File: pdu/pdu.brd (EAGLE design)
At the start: 0 parts

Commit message: import outline from fusion, add mounts
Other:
- board outline added: 17.5 x 90 mm
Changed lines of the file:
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@@
 <setting verticaltext="up"/>
 </settings>
-<grid distance="50" unitdist="mil" unit="mil" style="lines" multiple="1" display="no" altdistance="5" altunitdist="mil" altunit="mil"/>
+<grid distance="50" unitdist="mil" unit="mil" style="lines" multiple="1" display="yes" altdistance="5" altunitdist="mil" altunit="mil"/>
 <layers>
 <layer number="1" name="Top" color="4" fill="1" visible="yes" active="yes"/>
@@
 <layer number="18" name="Vias" color="2" fill="1" visible="yes" active="yes"/>
 <layer number="19" name="Unrouted" color="6" fill="1" visible="yes" active="yes"/>
-<layer number="20" name="Dimension" color="24" fill="1" visible="yes" active="yes"/>
-<layer number="21" name="tPlace" color="7" fill="1" visible="yes" active="yes"/>
-<layer number="22" name="bPlace" color="7" fill="1" visible="yes" active="yes"/>
+<layer number="20" name="Dimension" color="15" fill="1" visible="yes" active="yes"/>
+<layer number="21" name="tPlace" color="16" fill="1" visible="yes" active="yes"/>
+<layer number="22" name="bPlace" color="14" fill="1" visible="yes" active="yes"/>
 <layer number="23" name="tOrigins" color="15" fill="1" visible="yes" active="yes"/>
 <layer number="24" name="bOrigins" color="15" fill="1" visible="yes" active="yes"/>
-<layer number="25" name="tNames" color="7" fill="1" visible="yes" active="yes"/>
-<layer number="26" name="bNames" color="7" fill="1" visible="yes" active="yes"/>
-<layer number="27" name="tValues" color="7" fill="1" visible="yes" active="yes"/>
-<layer number="28" name="bValues" color="7" fill="1" visible="yes" active="yes"/>
+<layer number="25" name="tNames" color="7" fill="1" visible="no" active="yes"/>
+<layer number="26" name="bNames" color="7" fill="1" visible="no" active="yes"/>
+<layer number="27" name="tValues" color="7" fill="1" visible="no" active="yes"/>
+<layer number="28" name="bValues" color="7" fill="1" visible="no" active="yes"/>
 <layer number="29" name="tStop" color="7" fill="3" visible="no" active="yes"/>
 <layer number="30" name="bStop" color="7" fill="6" visible="no" active="yes"/>
@@
 <layer number="37" name="tTest" color="7" fill="1" visible="no" active="yes"/>
 <layer number="38" name="bTest" color="7" fill="1" visible="no" active="yes"/>
-<layer number="39" name="tKeepout" color="4" fill="11" visible="yes" active="yes"/>
-<layer number="40" name="bKeepout" color="1" fill="11" visible="yes" active="yes"/>
-<layer number="41" name="tRestrict" color="4" fill="10" visible="yes" active="yes"/>
-<layer number="42" name="bRestrict" color="1" fill="10" visible="yes" active="yes"/>
-<layer number="43" name="vRestrict" color="2" fill="10" visible="yes" active="yes"/>
+<layer number="39" name="tKeepout" color="4" fill="11" visible="no" active="yes"/>
+<layer number="40" name="bKeepout" color="1" fill="11" visible="no" active="yes"/>
+<layer number="41" name="tRestrict" color="4" fill="10" visible="no" active="yes"/>
+<layer number="42" name="bRestrict" color="1" fill="10" visible="no" active="yes"/>
+<layer number="43" name="vRestrict" color="2" fill="10" visible="no" active="yes"/>
 <layer number="44" name="Drills" color="7" fill="1" visible="no" active="yes"/>
-<layer number="45" name="Holes" color="7" fill="1" visible="no" active="yes"/>
+<layer number="45" name="Holes" color="7" fill="1" visible="yes" active="yes"/>
 <layer number="46" name="Milling" color="3" fill="1" visible="no" active="yes"/>
 <layer number="47" name="Measures" color="7" fill="1" visible="no" active="yes"/>
-<layer number="48" name="Document" color="7" fill="1" visible="yes" active="yes"/>
-<layer number="49" name="Reference" color="7" fill="1" visible="yes" active="yes"/>
-<layer number="51" name="tDocu" color="7" fill="1" visible="yes" active="yes"/>
-<layer number="52" name="bDocu" color="7" fill="1" visible="yes" active="yes"/>
+<layer number="48" name="Document" color="7" fill="1" visible="no" active="yes"/>
+<layer number="49" name="Reference" color="7" fill="1" visible="no" active="yes"/>
+<layer number="51" name="tDocu" color="6" fill="1" visible="yes" active="yes"/>
+<layer number="52" name="bDocu" color="7" fill="1" visible="no" active="yes"/>
 <layer number="88" name="SimResults" color="9" fill="1" visible="no" active="no"/>
 <layer number="89" name="SimProbes" color="9" fill="1" visible="no" active="no"/>
@@
 <board>
 <plain>
+<wire x1="8.75" y1="-45" x2="-8.75" y2="-45" width="0.254" layer="20"/>
+<wire x1="-8.75" y1="-45" x2="-8.75" y2="45" width="0.254" layer="20"/>
+<wire x1="-8.75" y1="45" x2="8.75" y2="45" width="0.254" layer="20"/>
+<wire x1="8.75" y1="45" x2="8.75" y2="-45" width="0.254" layer="20"/>
+<hole x="0" y="40" drill="4.2"/>
+<hole x="0" y="30" drill="4.2"/>
+<hole x="0" y="-40" drill="4.2"/>
 </plain>
 <attributes>

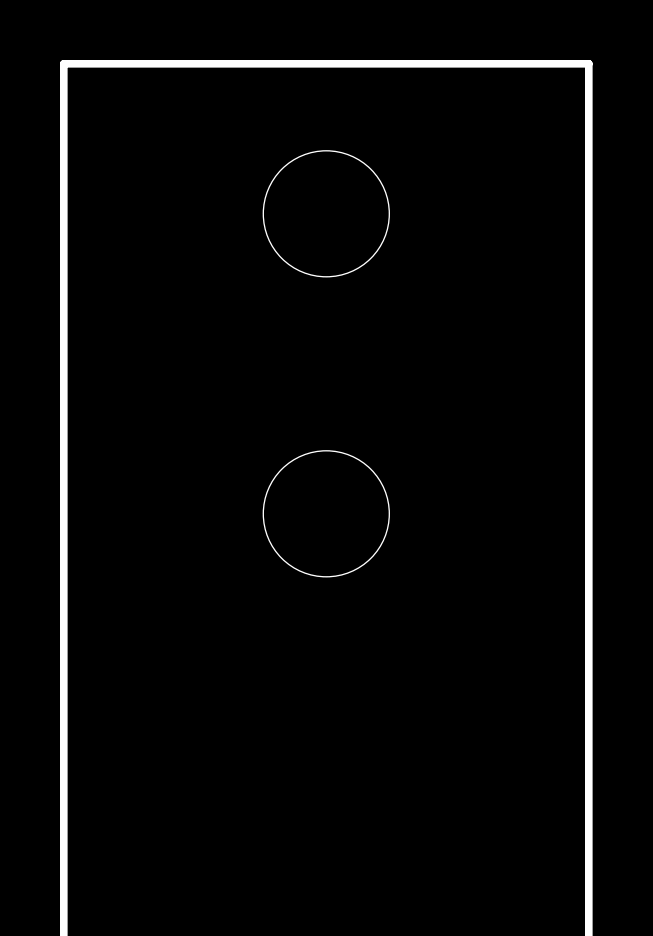
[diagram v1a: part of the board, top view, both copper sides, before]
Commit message: 3 bat inputs
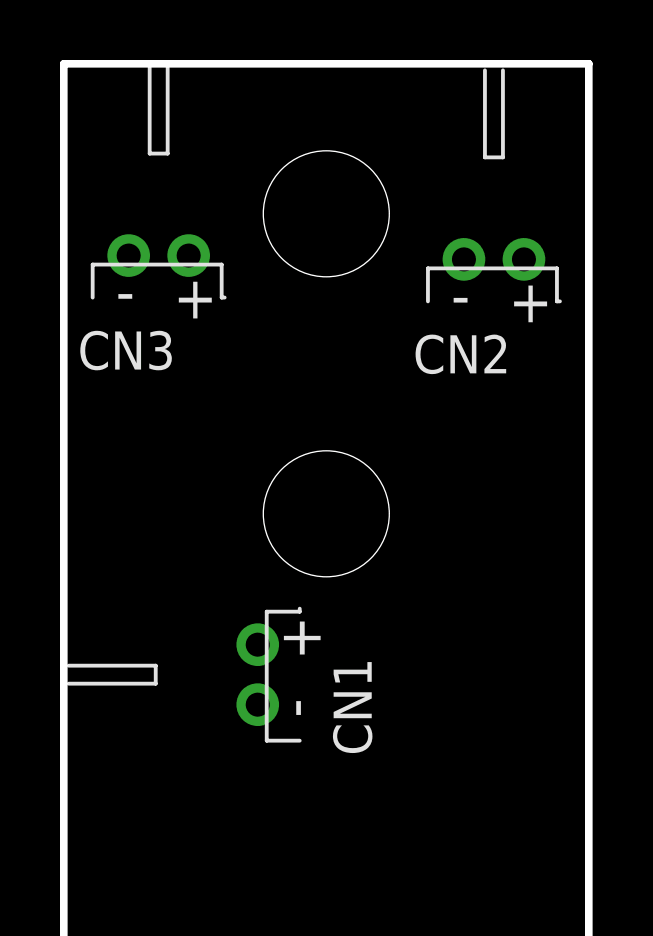
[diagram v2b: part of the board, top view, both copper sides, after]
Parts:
- added CN1, CN2, CN3: (no value), adafruit:JST-PH-2-THM-RA
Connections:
- new net GND: CN1.1, CN2.1, CN3.1
- new net VBAT: CN1.2, CN2.2, CN3.2
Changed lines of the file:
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@@
 <layer number="48" name="Document" color="7" fill="1" visible="no" active="yes"/>
 <layer number="49" name="Reference" color="7" fill="1" visible="no" active="yes"/>
+<layer number="50" name="dxf" color="7" fill="1" visible="no" active="yes"/>
 <layer number="51" name="tDocu" color="6" fill="1" visible="yes" active="yes"/>
 <layer number="52" name="bDocu" color="7" fill="1" visible="no" active="yes"/>
+<layer number="53" name="tGND_GNDA" color="7" fill="9" visible="no" active="no"/>
+<layer number="54" name="bGND_GNDA" color="1" fill="9" visible="no" active="no"/>
+<layer number="56" name="wert" color="7" fill="1" visible="no" active="yes"/>
+<layer number="57" name="tCAD" color="7" fill="1" visible="no" active="no"/>
+<layer number="59" name="tCarbon" color="7" fill="1" visible="no" active="no"/>
+<layer number="60" name="bCarbon" color="7" fill="1" visible="no" active="no"/>
 <layer number="88" name="SimResults" color="9" fill="1" visible="no" active="no"/>
 <layer number="89" name="SimProbes" color="9" fill="1" visible="no" active="no"/>
@@
 <layer number="97" name="Info" color="7" fill="1" visible="no" active="no"/>
 <layer number="98" name="Guide" color="6" fill="1" visible="no" active="no"/>
+<layer number="99" name="SpiceOrder" color="7" fill="1" visible="no" active="no"/>
+<layer number="100" name="Muster" color="7" fill="1" visible="no" active="no"/>
+<layer number="101" name="Patch_Top" color="12" fill="4" visible="no" active="yes"/>
+<layer number="102" name="Vscore" color="7" fill="1" visible="no" active="yes"/>
+<layer number="103" name="fp3" color="7" fill="1" visible="no" active="yes"/>
+<layer number="104" name="Name" color="7" fill="1" visible="no" active="yes"/>
+<layer number="105" name="Beschreib" color="9" fill="1" visible="no" active="yes"/>
+<layer number="106" name="BGA-Top" color="4" fill="1" visible="no" active="yes"/>
+<layer number="107" name="BD-Top" color="5" fill="1" visible="no" active="yes"/>
+<layer number="108" name="fp8" color="7" fill="1" visible="no" active="yes"/>
+<layer number="109" name="fp9" color="7" fill="1" visible="no" active="yes"/>
+<layer number="110" name="fp0" color="7" fill="1" visible="no" active="yes"/>
+<layer number="111" name="LPC17xx" color="7" fill="1" visible="no" active="yes"/>
+<layer number="112" name="tSilk" color="7" fill="1" visible="no" active="yes"/>
+<layer number="113" name="ReferenceLS" color="7" fill="1" visible="no" active="no"/>
+<layer number="116" name="Patch_BOT" color="9" fill="4" visible="no" active="yes"/>
+<layer number="118" name="Rect_Pads" color="7" fill="1" visible="no" active="no"/>
+<layer number="121" name="_tsilk" color="7" fill="1" visible="no" active="yes"/>
+<layer number="122" name="_bsilk" color="7" fill="1" visible="no" active="yes"/>
+<layer number="123" name="tTestmark" color="7" fill="1" visible="no" active="yes"/>
+<layer number="124" name="bTestmark" color="7" fill="1" visible="no" active="yes"/>
+<layer number="125" name="_tNames" color="7" fill="1" visible="no" active="yes"/>
+<layer number="126" name="_bNames" color="7" fill="1" visible="no" active="yes"/>
+<layer number="127" name="_tValues" color="7" fill="1" visible="no" active="yes"/>
+<layer number="128" name="_bValues" color="7" fill="1" visible="no" active="yes"/>
+<layer number="129" name="Mask" color="7" fill="1" visible="yes" active="yes"/>
+<layer number="131" name="tAdjust" color="7" fill="1" visible="no" active="yes"/>
+<layer number="132" name="bAdjust" color="7" fill="1" visible="no" active="yes"/>
+<layer number="144" name="Drill_legend" color="7" fill="1" visible="no" active="yes"/>
+<layer number="150" name="Notes" color="7" fill="1" visible="no" active="yes"/>
+<layer number="151" name="HeatSink" color="7" fill="1" visible="no" active="yes"/>
+<layer number="152" name="_bDocu" color="7" fill="1" visible="no" active="yes"/>
+<layer number="153" name="FabDoc1" color="6" fill="1" visible="no" active="no"/>
+<layer number="154" name="FabDoc2" color="2" fill="1" visible="no" active="no"/>
+<layer number="155" name="FabDoc3" color="7" fill="15" visible="no" active="no"/>
+<layer number="199" name="Contour" color="7" fill="1" visible="no" active="yes"/>
+<layer number="200" name="200bmp" color="1" fill="10" visible="no" active="yes"/>
+<layer number="201" name="201bmp" color="2" fill="1" visible="no" active="no"/>
+<layer number="202" name="202bmp" color="3" fill="1" visible="no" active="no"/>
+<layer number="203" name="203bmp" color="4" fill="10" visible="no" active="yes"/>
+<layer number="204" name="204bmp" color="5" fill="10" visible="no" active="yes"/>
+<layer number="205" name="205bmp" color="6" fill="10" visible="no" active="yes"/>
+<layer number="206" name="206bmp" color="7" fill="10" visible="no" active="yes"/>
+<layer number="207" name="207bmp" color="8" fill="10" visible="no" active="yes"/>
+<layer number="208" name="208bmp" color="9" fill="10" visible="no" active="yes"/>
+<layer number="209" name="209bmp" color="7" fill="1" visible="no" active="yes"/>
+<layer number="210" name="210bmp" color="7" fill="1" visible="no" active="yes"/>
+<layer number="211" name="211bmp" color="7" fill="1" visible="no" active="yes"/>
+<layer number="212" name="212bmp" color="7" fill="1" visible="no" active="yes"/>
+<layer number="213" name="213bmp" color="7" fill="1" visible="no" active="yes"/>
+<layer number="214" name="214bmp" color="7" fill="1" visible="no" active="yes"/>
+<layer number="215" name="215bmp" color="7" fill="1" visible="no" active="yes"/>
+<layer number="216" name="216bmp" color="7" fill="1" visible="no" active="yes"/>
+<layer number="217" name="217bmp" color="18" fill="1" visible="no" active="no"/>
+<layer number="218" name="218bmp" color="19" fill="1" visible="no" active="no"/>
+<layer number="219" name="219bmp" color="20" fill="1" visible="no" active="no"/>
+<layer number="220" name="220bmp" color="21" fill="1" visible="no" active="no"/>
+<layer number="221" name="221bmp" color="22" fill="1" visible="no" active="no"/>
+<layer number="222" name="222bmp" color="23" fill="1" visible="no" active="no"/>
+<layer number="223" name="223bmp" color="24" fill="1" visible="no" active="no"/>
+<layer number="224" name="224bmp" color="25" fill="1" visible="no" active="no"/>
+<layer number="225" name="225bmp" color="7" fill="1" visible="yes" active="yes"/>
+<layer number="226" name="226bmp" color="7" fill="1" visible="yes" active="yes"/>
+<layer number="227" name="227bmp" color="7" fill="1" visible="yes" active="yes"/>
+<layer number="228" name="228bmp" color="7" fill="1" visible="yes" active="yes"/>
+<layer number="229" name="229bmp" color="7" fill="1" visible="yes" active="yes"/>
+<layer number="230" name="230bmp" color="7" fill="1" visible="yes" active="yes"/>
+<layer number="231" name="Eagle3D_PG1" color="7" fill="1" visible="no" active="no"/>
+<layer number="232" name="Eagle3D_PG2" color="7" fill="1" visible="no" active="no"/>
+<layer number="233" name="Eagle3D_PG3" color="7" fill="1" visible="no" active="no"/>
+<layer number="248" name="Housing" color="7" fill="1" visible="no" active="yes"/>
+<layer number="249" name="Edge" color="7" fill="1" visible="no" active="yes"/>
+<layer number="250" name="Descript" color="7" fill="1" visible="no" active="no"/>
+<layer number="251" name="SMDround" color="7" fill="1" visible="no" active="no"/>
+<layer number="254" name="cooling" color="7" fill="1" visible="no" active="yes"/>
+<layer number="255" name="routoute" color="7" fill="1" visible="yes" active="yes"/>
 </layers>
 <board>
@@
 </autorouter>
 <elements>
+<element name="CN1" library="adafruit" library_urn="urn:adsk.eagle:library:420" package="JST-PH-2-THM-RA" package3d_urn="urn:adsk.eagle:package:6240694/1" value="" x="-2.286" y="24.638" smashed="yes" rot="R90">
+<attribute name="NAME" x="1.514" y="21.938" size="1.27" layer="25" font="vector" rot="R90"/>
+</element>
+<element name="CN2" library="adafruit" library_urn="urn:adsk.eagle:library:420" package="JST-PH-2-THM-RA" package3d_urn="urn:adsk.eagle:package:6240694/1" value="" x="5.588" y="38.481" smashed="yes">
+<attribute name="NAME" x="2.888" y="34.681" size="1.27" layer="25" font="vector"/>
+</element>
+<element name="CN3" library="adafruit" library_urn="urn:adsk.eagle:library:420" package="JST-PH-2-THM-RA" package3d_urn="urn:adsk.eagle:package:6240694/1" value="" x="-5.588" y="38.608" smashed="yes">
+<attribute name="NAME" x="-8.288" y="34.808" size="1.27" layer="25" font="vector"/>
+</element>
 </elements>
 <signals>
+<signal name="GND">
+<contactref element="CN1" pad="1"/>
+<contactref element="CN2" pad="1"/>
+<contactref element="CN3" pad="1"/>
+<wire x1="6.588" y1="38.481" x2="-4.588" y2="38.608" width="0" layer="19" extent="1-1"/>
+<wire x1="-2.286" y1="25.638" x2="6.588" y2="38.481" width="0" layer="19" extent="1-1"/>
+</signal>
+<signal name="VBAT">
+<contactref element="CN3" pad="2"/>
+<contactref element="CN1" pad="2"/>
+<contactref element="CN2" pad="2"/>
+<wire x1="4.588" y1="38.481" x2="-6.588" y2="38.608" width="0" layer="19" extent="1-1"/>
+<wire x1="-2.286" y1="23.638" x2="4.588" y2="38.481" width="0" layer="19" extent="1-1"/>
+</signal>
 </signals>
 <mfgpreviewcolors>
@@
 </board>
 </drawing>
+<compatibility>
+<note version="8.2" severity="warning">
+Since Version 8.2, EAGLE supports online libraries. The ids
+of those online libraries will not be understood (or retained)
+with this version.
+</note>
+<note version="8.3" severity="warning">
+Since Version 8.3, EAGLE supports URNs for individual library
+assets (packages, symbols, and devices). The URNs of those assets
+will not be understood (or retained) with this version.
+</note>
+<note version="8.3" severity="warning">
+Since Version 8.3, EAGLE supports the association of 3D packages
+with devices in libraries, schematics, and board files. Those 3D
+packages will not be understood (or retained) with this version.
+</note>
+</compatibility>
 </eagle>

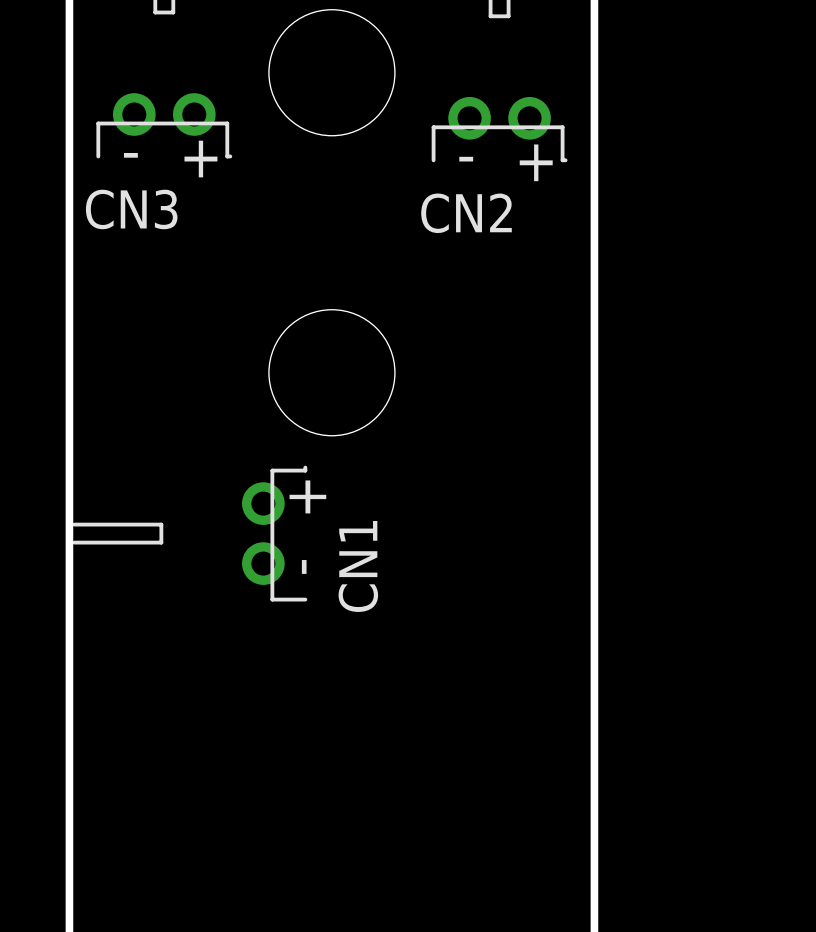
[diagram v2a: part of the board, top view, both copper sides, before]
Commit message: initial mosfet with RC
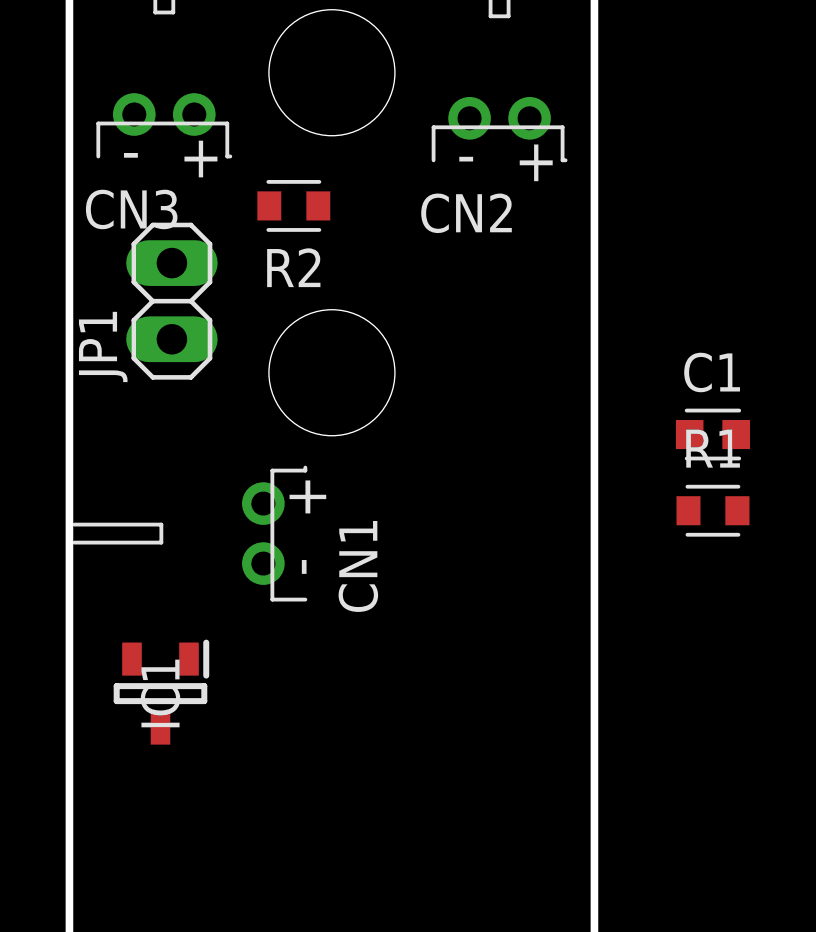
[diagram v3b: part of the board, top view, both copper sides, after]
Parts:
- added C1: 100p, Capacitor:CAPC1608X85
- added IC1: FDN359BN, SamacSys_Parts:SOT95P251X112-3N
- added JP1: PINHD-1X2, Connector:1X02
- added R1: 470, Resistor:RESC1608X60
- added R2: 68k, Resistor:RESC1608X60
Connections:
- new net EN: JP1.2, R1.2, R2.2
- new net N$1: C1.2, IC1.1, R1.1
- net GND: now also C1.1, IC1.2, R2.1
- net VBAT: now also JP1.1
